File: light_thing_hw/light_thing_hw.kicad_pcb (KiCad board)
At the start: 2 copper layers, 50 x 50 mm, 53 parts, among them J1 CONNECTORS, J2 Li-Ion Battery, J3 ADDR_LED_PANEL_1_CONNECTORS, J4 ADDR_LED_PANEL_2_CONNECTORS, Q1 MMBF170, SW1 ST_USER_BUTTON1, SW2 ST_RESET_BUTTON, U1 BC832-V1, U2 LSM6DS3, U3 MCP73833T-FCI_UN, U4 LMR62421XMF, U5 LP38511MRX, U5A1 STM32L452RETx

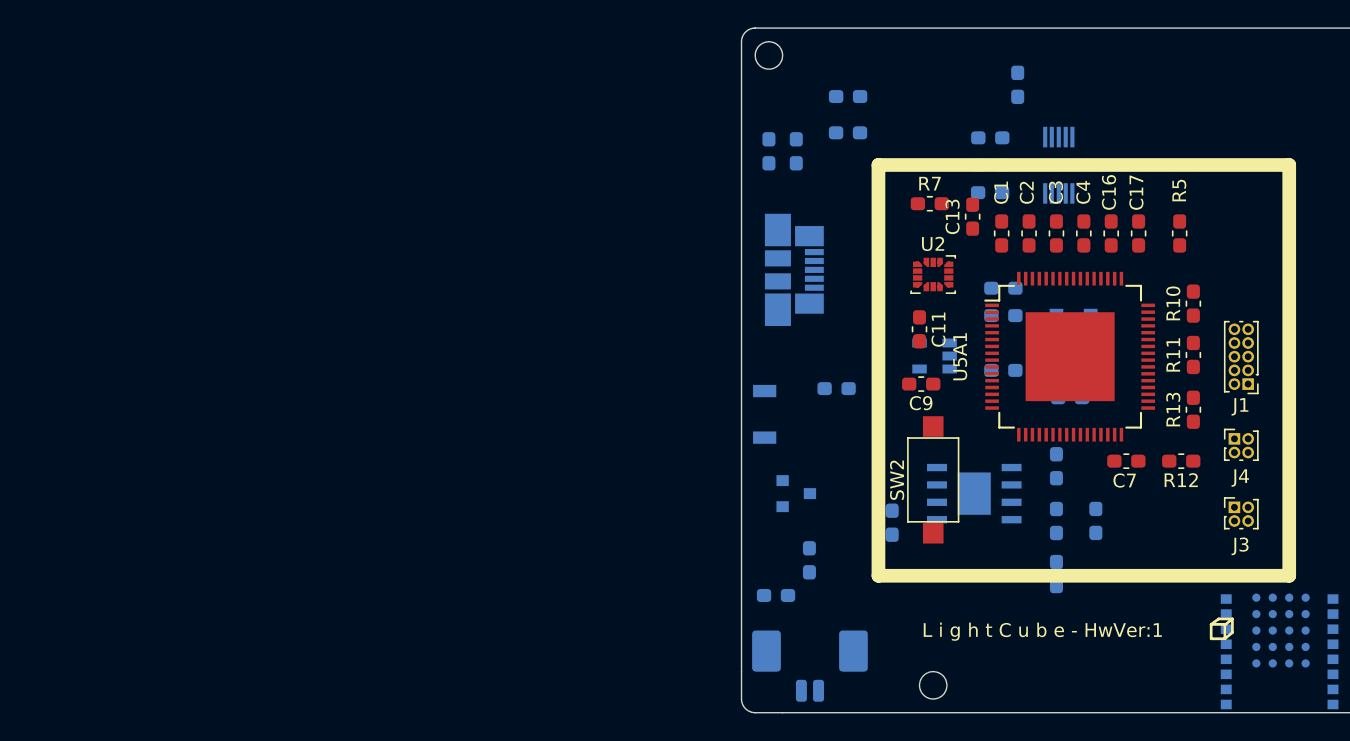
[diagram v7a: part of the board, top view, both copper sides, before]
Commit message: gonna make the vvias now
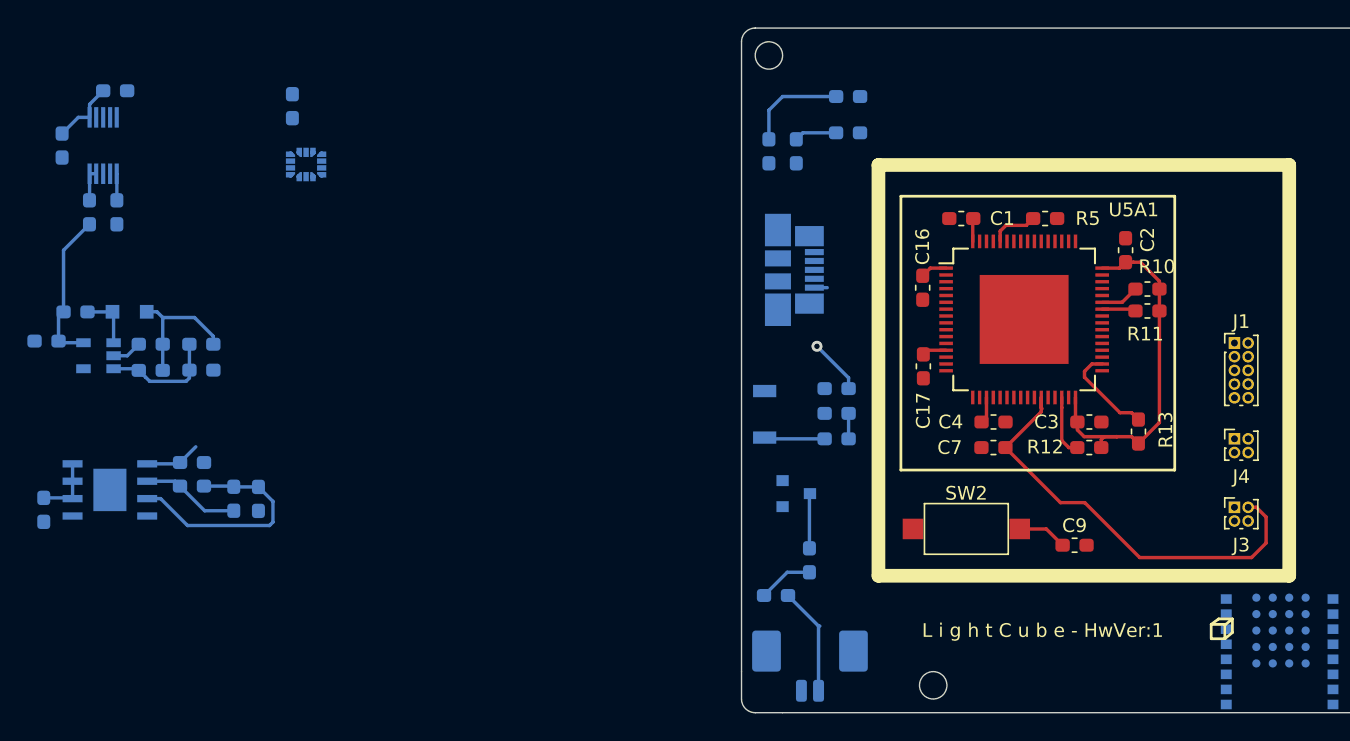
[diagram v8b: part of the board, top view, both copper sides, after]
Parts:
- C11, C13, R7, U2: moved to B.Cu
- moved C8 70.0 mm to (56.2, 78.9), turned to 0 degrees
- moved C5 69.9 mm to (57.4, 64.6), turned to 270 degrees
- moved U3 69.8 mm to (60.4, 64.6)
- moved D1 68.9 mm to (62.3, 76.7)
- moved L1 67.8 mm to (58.4, 76.7)
- moved C12 67.2 mm to (63.9, 81.0)
- moved C15 66.1 mm to (66.9, 89.5), turned to 180 degrees
- moved C6 65.8 mm to (59.4, 69.5), turned to 90 degrees
- moved R1 64.0 mm to (61.3, 60.6), turned to 0 degrees
- moved R17 63.9 mm to (61.4, 69.5), turned to 90 degrees
- moved R3 63.5 mm to (67.5, 79.1)
- moved R4 63.5 mm to (67.6, 81.0)
- moved U5 63.1 mm to (60.9, 89.7)
- moved C18 63.1 mm to (66.9, 87.7), turned to 180 degrees
- moved C10 62.3 mm to (63.9, 79.1)
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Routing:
- net +3V3: track 0.00 -> 49.2 mm, vias 0 -> 1
- net ADDR_LED_PANEL_1_PWM: track 0.00 -> 31.9 mm
- net +BATT: track 0.00 -> 24.0 mm
- net Net-(C15-Pad1): track 0.00 -> 17.1 mm
- net +5V: track 0.00 -> 10.0 mm
- net Net-(C12-Pad2): track 0.00 -> 8.49 mm
- net Net-(D2-Pad2): track 0.00 -> 7.45 mm
- net I2C2_SCL: track 0.00 -> 7.16 mm
- net VBUS: track 0.00 -> 5.79 mm
- net I2C2_SDA: track 0.00 -> 4.49 mm
- net BUTTON1: track 0.00 -> 4.42 mm
- net Net-(D1-Pad2): track 0.00 -> 4.12 mm
- net BATT_ADC: track 0.00 -> 4.02 mm
- net Net-(Q1-Pad3): track 0.00 -> 3.95 mm
- net RESET: track 0.00 -> 3.62 mm
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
